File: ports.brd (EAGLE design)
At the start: 24 x 10 mm, 3 parts

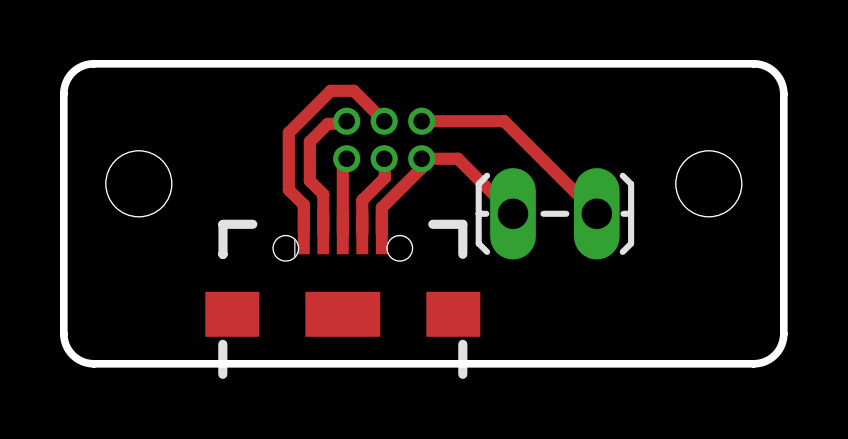
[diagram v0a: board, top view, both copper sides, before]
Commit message: Widened copper around Gecko connector holes
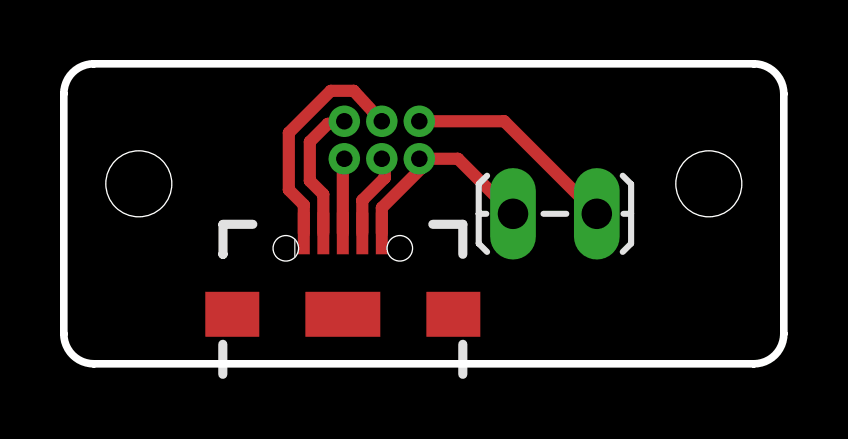
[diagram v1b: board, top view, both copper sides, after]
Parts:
- moved U$1 3.20 mm to (10.6, 5.00)
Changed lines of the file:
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@@
 </element>
 <element name="JP1" library="SparkFun-Connectors" package="1X02_LOCK_LONGPADS" value="M02LOCK_LONGPADS" x="15.1" y="5" smashed="yes"/>
-<element name="U$1" library="G125-FV20605L0P" package="G125-FV20605L0P" value="G125-FV20605L0P" x="13.8" y="5" smashed="yes" rot="MR0"/>
+<element name="U$1" library="G125-FV20605L0P" package="G125-FV20605L0P" value="G125-FV20605L0P" x="10.6" y="5" smashed="yes" rot="MR0"/>
 </elements>
 <signals>
@@
 <contactref element="U$1" pad="P4"/>
 <contactref element="JP1" pad="1"/>
-<wire x1="11.93" y1="6.835" x2="13.138" y2="6.835" width="0.4064" layer="1"/>
+<wire x1="11.85" y1="6.835" x2="13.138" y2="6.835" width="0.4064" layer="1"/>
 <wire x1="13.138" y1="6.835" x2="14.973" y2="5" width="0.4064" layer="1"/>
-<wire x1="11.93" y1="6.835" x2="11.93" y2="6.53" width="0.4064" layer="1"/>
+<wire x1="11.85" y1="6.835" x2="11.93" y2="6.53" width="0.4064" layer="1"/>
 <wire x1="11.93" y1="6.53" x2="10.6" y2="5.2" width="0.4064" layer="1"/>
 <wire x1="10.6" y1="5.2" x2="10.6" y2="4.35" width="0.4064" layer="1"/>
@@
 <contactref element="U$1" pad="P6"/>
 <wire x1="9.3" y1="4.35" x2="9.3" y2="6.705" width="0.4064" layer="1"/>
-<wire x1="9.3" y1="6.705" x2="9.43" y2="6.835" width="0.4064" layer="1"/>
+<wire x1="9.3" y1="6.705" x2="9.35" y2="6.835" width="0.4064" layer="1"/>
 </signal>
 <signal name="D-">
@@
 <wire x1="8.2" y1="7.4" x2="8.8" y2="8" width="0.4064" layer="1"/>
 <wire x1="8.8" y1="8" x2="9.345" y2="8" width="0.4064" layer="1"/>
-<wire x1="9.345" y1="8" x2="9.43" y2="8.085" width="0.4064" layer="1"/>
+<wire x1="9.345" y1="8" x2="9.35" y2="8.085" width="0.4064" layer="1"/>
 </signal>
 <signal name="VBUS">
@@
 <wire x1="7.5" y1="7.7" x2="8.9" y2="9.1" width="0.4064" layer="1"/>
 <wire x1="8.9" y1="9.1" x2="9.665" y2="9.1" width="0.4064" layer="1"/>
-<wire x1="9.665" y1="9.1" x2="10.68" y2="8.085" width="0.4064" layer="1"/>
+<wire x1="9.665" y1="9.1" x2="10.6" y2="8.085" width="0.4064" layer="1"/>
 </signal>
 <signal name="ID">
@@
 <wire x1="9.95" y1="5.45" x2="10.7" y2="6.2" width="0.4064" layer="1"/>
 <wire x1="10.7" y1="6.2" x2="10.7" y2="6.815" width="0.4064" layer="1"/>
-<wire x1="10.7" y1="6.815" x2="10.68" y2="6.835" width="0.4064" layer="1"/>
+<wire x1="10.7" y1="6.815" x2="10.6" y2="6.835" width="0.4064" layer="1"/>
 </signal>
 <signal name="VBATT">
 <contactref element="JP1" pad="2"/>
 <contactref element="U$1" pad="P1"/>
-<wire x1="11.93" y1="8.085" x2="14.682" y2="8.085" width="0.4064" layer="1"/>
+<wire x1="11.85" y1="8.085" x2="14.682" y2="8.085" width="0.4064" layer="1"/>
 <wire x1="14.682" y1="8.085" x2="17.767" y2="5" width="0.4064" layer="1"/>
 </signal>

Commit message: Move Gecko connector on ports board in from edge
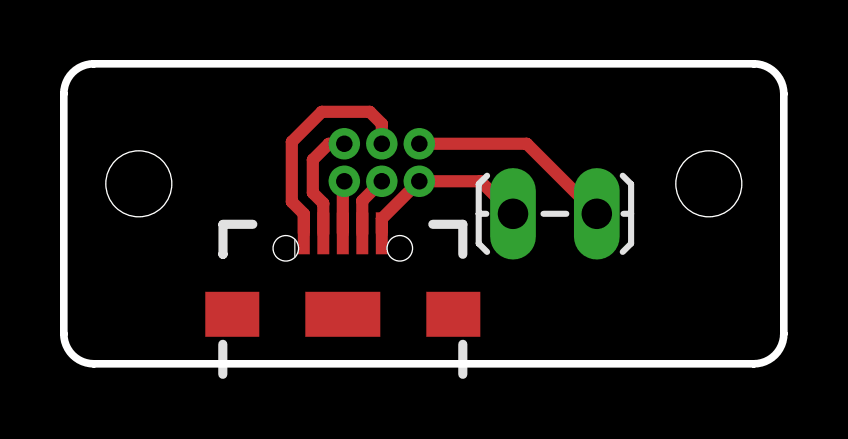
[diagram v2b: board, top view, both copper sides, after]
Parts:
- moved U$1 0.75 mm to (10.6, 4.25)
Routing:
- net GND: track 6.93 -> 5.83 mm
- net ID: track 2.88 -> 2.00 mm
- net D-: track 4.72 -> 3.87 mm
- net D+: track 2.49 -> 1.76 mm
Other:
- board text added: "KickSat Ports V1.1"
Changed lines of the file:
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@@
 <dimension x1="2.5" y1="6" x2="2.5" y2="0" x3="3.6" y3="3" textsize="1.778" layer="51" dtype="vertical"/>
 <dimension x1="21.5" y1="6" x2="24" y2="6" x3="22.75" y3="3" textsize="1.778" layer="51" dtype="horizontal"/>
+<text x="3.8" y="2.4" size="1.4224" layer="26" rot="SMR180">KickSat Ports V1.1</text>
 </plain>
 <attributes>
@@
 </element>
 <element name="JP1" library="SparkFun-Connectors" package="1X02_LOCK_LONGPADS" value="M02LOCK_LONGPADS" x="15.1" y="5" smashed="yes"/>
-<element name="U$1" library="G125-FV20605L0P" package="G125-FV20605L0P" value="G125-FV20605L0P" x="10.6" y="5" smashed="yes" rot="MR0"/>
+<element name="U$1" library="G125-FV20605L0P" package="G125-FV20605L0P" value="G125-FV20605L0P" x="10.6" y="4.25" smashed="yes" rot="MR0"/>
 </elements>
 <signals>
@@
 <contactref element="U$1" pad="P4"/>
 <contactref element="JP1" pad="1"/>
-<wire x1="11.85" y1="6.835" x2="13.138" y2="6.835" width="0.4064" layer="1"/>
-<wire x1="13.138" y1="6.835" x2="14.973" y2="5" width="0.4064" layer="1"/>
-<wire x1="11.85" y1="6.835" x2="11.93" y2="6.53" width="0.4064" layer="1"/>
-<wire x1="11.93" y1="6.53" x2="10.6" y2="5.2" width="0.4064" layer="1"/>
-<wire x1="10.6" y1="5.2" x2="10.6" y2="4.35" width="0.4064" layer="1"/>
+<wire x1="10.6" y1="4.35" x2="10.6" y2="4.835" width="0.4064" layer="1"/>
+<wire x1="10.6" y1="4.835" x2="11.85" y2="6.085" width="0.4064" layer="1"/>
+<wire x1="11.85" y1="6.085" x2="13.888" y2="6.085" width="0.4064" layer="1"/>
+<wire x1="13.888" y1="6.085" x2="14.973" y2="5" width="0.4064" layer="1"/>
 </signal>
 <signal name="D+">
 <contactref element="U$4" pad="D+1"/>
 <contactref element="U$1" pad="P6"/>
-<wire x1="9.3" y1="4.35" x2="9.3" y2="6.705" width="0.4064" layer="1"/>
-<wire x1="9.3" y1="6.705" x2="9.35" y2="6.835" width="0.4064" layer="1"/>
+<wire x1="9.3" y1="4.35" x2="9.3" y2="6.035" width="0.4064" layer="1"/>
+<wire x1="9.3" y1="6.035" x2="9.35" y2="6.085" width="0.4064" layer="1"/>
 </signal>
 <signal name="D-">
 <contactref element="U$4" pad="D-1"/>
 <contactref element="U$1" pad="P3"/>
-<wire x1="8.65" y1="4.35" x2="8.65" y2="5.65" width="0.4064" layer="1"/>
-<wire x1="8.65" y1="5.65" x2="8.2" y2="6.1" width="0.4064" layer="1"/>
-<wire x1="8.2" y1="6.1" x2="8.2" y2="7.4" width="0.4064" layer="1"/>
-<wire x1="8.2" y1="7.4" x2="8.8" y2="8" width="0.4064" layer="1"/>
-<wire x1="8.8" y1="8" x2="9.345" y2="8" width="0.4064" layer="1"/>
-<wire x1="9.345" y1="8" x2="9.35" y2="8.085" width="0.4064" layer="1"/>
+<wire x1="8.65" y1="4.35" x2="8.65" y2="5.35" width="0.4064" layer="1"/>
+<wire x1="8.65" y1="5.35" x2="8.3" y2="5.7" width="0.4064" layer="1"/>
+<wire x1="9.35" y1="7.335" x2="8.835" y2="7.335" width="0.4064" layer="1"/>
+<wire x1="8.835" y1="7.335" x2="8.3" y2="6.8" width="0.4064" layer="1"/>
+<wire x1="8.3" y1="6.8" x2="8.3" y2="5.7" width="0.4064" layer="1"/>
 </signal>
 <signal name="VBUS">
 <contactref element="U$4" pad="VBUS1"/>
 <contactref element="U$1" pad="P2"/>
-<wire x1="8" y1="4.35" x2="8" y2="5.3" width="0.4064" layer="1"/>
-<wire x1="8" y1="5.3" x2="7.5" y2="5.8" width="0.4064" layer="1"/>
-<wire x1="7.5" y1="5.8" x2="7.5" y2="7.7" width="0.4064" layer="1"/>
-<wire x1="7.5" y1="7.7" x2="8.9" y2="9.1" width="0.4064" layer="1"/>
-<wire x1="8.9" y1="9.1" x2="9.665" y2="9.1" width="0.4064" layer="1"/>
-<wire x1="9.665" y1="9.1" x2="10.6" y2="8.085" width="0.4064" layer="1"/>
+<wire x1="8" y1="4.35" x2="8" y2="5" width="0.4064" layer="1"/>
+<wire x1="8" y1="5" x2="7.6" y2="5.4" width="0.4064" layer="1"/>
+<wire x1="7.6" y1="5.4" x2="7.6" y2="7.4" width="0.4064" layer="1"/>
+<wire x1="7.6" y1="7.4" x2="8.6" y2="8.4" width="0.4064" layer="1"/>
+<wire x1="8.6" y1="8.4" x2="10.2" y2="8.4" width="0.4064" layer="1"/>
+<wire x1="10.2" y1="8.4" x2="10.6" y2="8" width="0.4064" layer="1"/>
+<wire x1="10.6" y1="8" x2="10.6" y2="7.335" width="0.4064" layer="1"/>
 </signal>
 <signal name="ID">
 <contactref element="U$4" pad="ID1"/>
 <contactref element="U$1" pad="P5"/>
-<wire x1="9.95" y1="4.35" x2="9.95" y2="5.45" width="0.4064" layer="1"/>
-<wire x1="9.95" y1="5.45" x2="10.7" y2="6.2" width="0.4064" layer="1"/>
-<wire x1="10.7" y1="6.2" x2="10.7" y2="6.815" width="0.4064" layer="1"/>
-<wire x1="10.7" y1="6.815" x2="10.6" y2="6.835" width="0.4064" layer="1"/>
+<wire x1="9.95" y1="4.35" x2="9.95" y2="5.435" width="0.4064" layer="1"/>
+<wire x1="9.95" y1="5.435" x2="10.6" y2="6.085" width="0.4064" layer="1"/>
 </signal>
 <signal name="VBATT">
 <contactref element="JP1" pad="2"/>
 <contactref element="U$1" pad="P1"/>
-<wire x1="11.85" y1="8.085" x2="14.682" y2="8.085" width="0.4064" layer="1"/>
-<wire x1="14.682" y1="8.085" x2="17.767" y2="5" width="0.4064" layer="1"/>
+<wire x1="11.85" y1="7.335" x2="15.432" y2="7.335" width="0.4064" layer="1"/>
+<wire x1="15.432" y1="7.335" x2="17.767" y2="5" width="0.4064" layer="1"/>
 </signal>
 </signals>
